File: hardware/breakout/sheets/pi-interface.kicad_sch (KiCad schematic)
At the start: 25 parts, among them J10 Barcode spare 1, J11 Barcode spare 2, J12 Barcode spare 3, J13 Dual panel BNC: Eye camera sy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, J15 Dual panel BNC: Behavior came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, J17 Dual panel BNC: Behavior came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, J18 Internal USB-A (sync-module p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, J7 Sync-module 40-pin GPIO heade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, J8 Barcode -> NI optocoupler (Ta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, J9 Barcode -> Intan optocoupler 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, U14 SN74LVC541APW, U15 SN74AHCT541PW, U74 SN74AHCT541PW

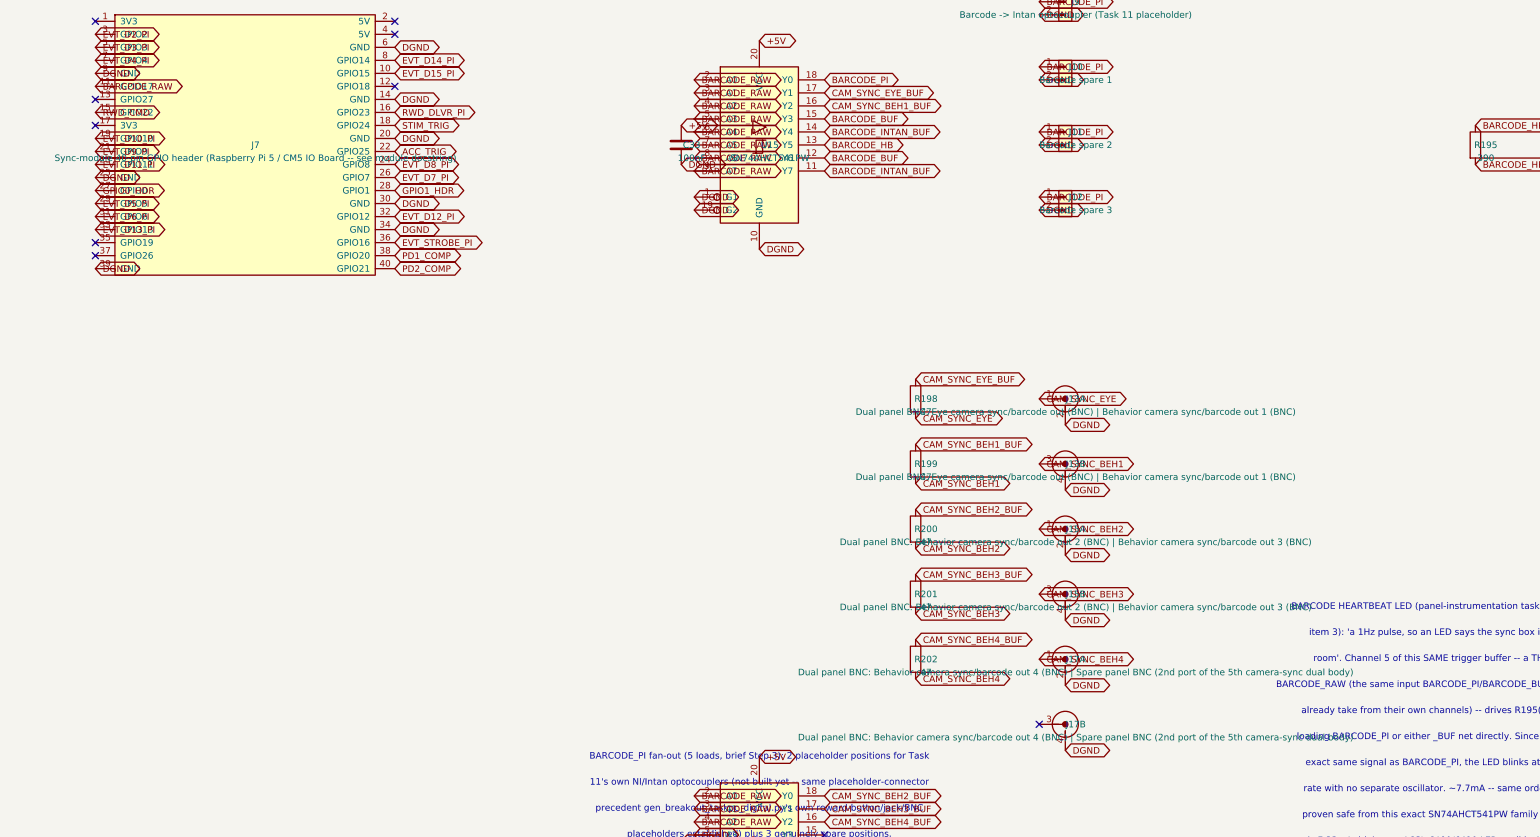
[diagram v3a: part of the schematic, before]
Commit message: feat(hardware): frame-time inputs -- camera strobes back to GPIO26/27
Closes the gap camera-sync-change.md §3 opened. With the cameras free-running,
spec §12 item 1's justification for dropping exposure-active returns ("the Pi
triggers the cameras so frame times are known by construction") is false in
both halves. One FLIR ExposureActive strobe per camera group now returns on a
spare back-panel BNC and is timestamped in the same event stream as everything
else.

WHY A COMPARATOR AND NOT THIS BOARD'S USUAL INBOUND BUFFER. The strobe's best
published low is 0.87 V against SN74LVC541A's 0.8 V V_IL max -- a SILENT 70 mV
miss, on a signal that looks perfectly correct on a scope. A comparator is also
the only option here whose margin is a design choice rather than a datasheet
coincidence, which matters because FLIR label the whole table "values are for
reference only".

WHY +12V AND NOT +5V. The LM339's input common-mode ceiling is V+ - 1.5V to
V+ - 2.0V. The strobe's HIGH is 5.0 V (pulled up to +5V through 1k, FLIR's own
published row -- a stiffer pull-up makes V_low worse, not better). On a +5V
supply that ceiling is 3.0-3.5 V and the input sits above it, which is the
LM339's best-known failure mode. +12V/AGND matches U54 exactly.

GROUND DOMAINS, WHICH THE FIRST PASS GOT BACKWARDS. The pull-up sources from
+5V, whose return is DGND, so the shell net decides where 4.2 mA of switching
current flows: on AGND it would cross NT1, the single star tie, on every camera
frame; on DGND it never does. Shells, clamps and the threshold divider are
therefore DGND. V- stays AGND and does not enter the comparison -- both inputs
are DGND-referenced, so the offset is common-mode and cancels -- it sets only
the output LOW level, exactly as it already does for PD1_COMP/PD2_COMP/ACC_TRIG.

Tying the spare sections' inputs to DGND made U76 a SECOND AGND/DGND bridge
alongside NT1; check_breakout_power_netlist.py caught it. They go to AGND, this
part's own V-. A negative control now reproduce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
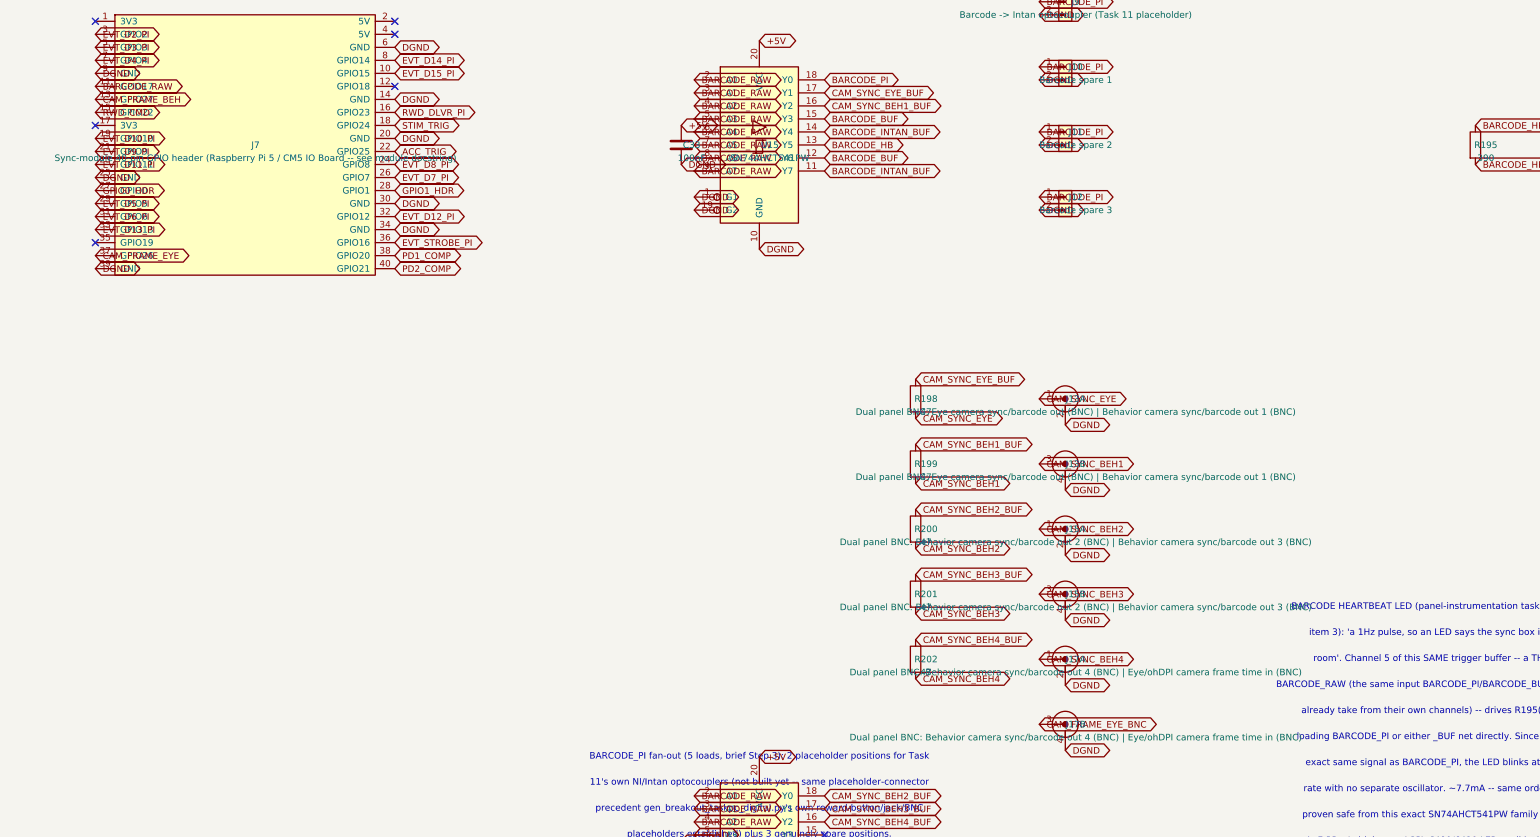
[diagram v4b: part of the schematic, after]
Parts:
- J17: value Dual panel BNC: Behavior camera sync/barcode out 4 (BNC) | Spare panel BNC (2nd port of the 5th camera-sync dual body) -> Dual panel BNC: Behavior camera sync/barcode out 4 (BNC) | Eye/ohDPI camera frame time in (BNC)
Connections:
- net CAM_FRAME_EYE_BNC: now reaches J17.3 (B_In)
- net CAM_FRAME_BEH: now reaches J7.13 (GPIO27)
- net CAM_FRAME_EYE: now reaches J7.37 (GPIO26)
- no-connect marks 21 -> 18
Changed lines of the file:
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@@
 		)
 	)
-	(no_connect
-		(at 170.17999999999998 181.61)
-	)
-	(no_connect
-		(at 170.17999999999998 151.13000000000002)
+	(global_label "CAM_FRAME_EYE"
+		(shape bidirectional)
+		(at 170.17999999999998 181.61 0)
+		(effects (font (size 1.27 1.27)) (justify left))
+		(property "Intersheetrefs" "${INTERSHEET_REFS}"
+			(at 170.17999999999998 181.61 0)
+			(effects (font (size 1.27 1.27)) (hide yes))
+		)
+	)
+	(global_label "CAM_FRAME_BEH"
+		(shape bidirectional)
+		(at 170.17999999999998 151.13000000000002 0)
+		(effects (font (size 1.27 1.27)) (justify left))
+		(property "Intersheetrefs" "${INTERSHEET_REFS}"
+			(at 170.17999999999998 151.13000000000002 0)
+			(effects (font (size 1.27 1.27)) (hide yes))
+		)
 	)
 	(text "Sync-module GPIO map (spec Sec.4 -- transcribed verbatim; restated here so this"
@@
 			(effects (font (size 1.27 1.27)))
 		)
-		(property "Value" "Dual panel BNC: Behavior camera sync/barcode out 4 (BNC) | Spare panel BNC (2nd port of the 5th camera-sync dual body)"
+		(property "Value" "Dual panel BNC: Behavior camera sync/barcode out 4 (BNC) | Eye/ohDPI camera frame time in (BNC)"
 			(at 361.442 262.89000000000004 0)
 			(effects (font (size 1.27 1.27)))
@@
 			(effects (font (size 1.27 1.27)))
 		)
-		(property "Value" "Dual panel BNC: Behavior camera sync/barcode out 4 (BNC) | Spare panel BNC (2nd port of the 5th camera-sync dual body)"
+		(property "Value" "Dual panel BNC: Behavior camera sync/barcode out 4 (BNC) | Eye/ohDPI camera frame time in (BNC)"
 			(at 361.442 275.59000000000003 0)
 			(effects (font (size 1.27 1.27)))
@@
 		)
 	)
-	(no_connect
-		(at 354.33000000000004 273.05)
-	)
-	(global_label "DGND"
+	(global_label "CAM_FRAME_EYE_BNC"
+		(shape bidirectional)
+		(at 354.33000000000004 273.05 0)
+		(effects (font (size 1.27 1.27)) (justify left))
+		(property "Intersheetrefs" "${INTERSHEET_REFS}"
+			(at 354.33000000000004 273.05 0)
+			(effects (font (size 1.27 1.27)) (hide yes))
+		)
+	)
+	(global_label "DGND"

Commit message: Breakout: draw the task-PC line-out and the PFI copy of PD1_COMP
Implements hardware/breakout/line-out-and-pfi-copy.md (spec Sec.12 item 11,
wl-xcon XC-327), approved 2026-10-18.

- Line-out. Connector 0's AO 0/AO 1 (pins 22/21) go through R221/R222
  (100 ohm) to J57, a new isolated dual BNC on the back face. Its shells are on
  AO_GND_TPC (pins 55/54) and nothing else: NI ties AO GND to D GND on the card,
  so no board plane may carry the amplifier's return.
- PFI copy. pi-interface's SN74LVC541A level shifter gains channel 1, PD1_COMP ->
  PD1_COMP_PFI_BUF, which R223 (100 ohm) takes to Connector 0 pin 38, PFI 7.
  That pin avoids the default counter outputs, PFI 12-15. The departure from
  spec Sec.7.1's direction table is stated where it is made.
- D3 was reversed while drawing. Tying Connector 0's D GND to DGND made it a
  second component on both grounds after the star-point net tie, because its
  AISENSE is on AGND. check_breakout_power_netlist.py caught it. Pin 36 stays
  no-connect, and the checker now asserts that.

New refdes are out of band (J57, R221-R223, above the J56/R220 maxima). Only the
two changed sheets were regenerated, and no existing refdes moved on either.

Checks:
- both sheet checkers gained exact node assertions plus four mutations
  (shell on DGND, L/R swapped, copy on PFI 8, copy fed from a tied-off input);
- all ten checkers pass with their self-tests;
- ERC is unchanged (0 errors, the same 3 warnings);
- the netlist export reports no annotation errors;
- the netlist contract and both BOMs are updated, with the BOM count guards
  bumped deliberately.

Also corrects the generator's claim that P2 is on Connector 1. Panel
elevations: the back face goes to 10 bodies with 7.2 mm of slack, so nothing
more fits there. The wl-xcon reply names PFI 7 and the never-an-output rule.

Co-Authored-By: Claude Opus 5.5 (1M context) <noreply@anthropic.com>
Claude-Session: https://claude.ai/code/session_013HK81J55qfjevPUUfGjAqJ
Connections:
- net DGND: no longer U14.3 (A1)
- net PD1_COMP: now also U14.3 (A1)
- net PD1_COMP_PFI_BUF: now reaches U14.17 (Y1)
- no-connect marks 18 -> 17
